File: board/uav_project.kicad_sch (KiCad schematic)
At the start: 0 parts

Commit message: Hopefully finished schema for pcb
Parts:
- added C14: 100n, symbol Device:C
- added D5: RCLAMP3328P, Package_DFN_QFN:UDFN-9_1.0x3.8mm_P0.5mm, symbol Power_Protection:RCLAMP3328P
- added J2: Conn_01x08_Pin, symbol Connector:Conn_01x08_Pin
- added R24, R25: 4.7k, symbol Device:R
- added WT901B1: ~, symbol .kicad_sym:WT901B
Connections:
- new net: D5.9 (K8), J2.8 (Pin_8)
- new net +3V3: C14.1, D5.8 (K7), J2.7 (Pin_7), R24.1, R25.1, WT901B1. (VCC)
- new net +5V: D5.7 (K6), J2.6 (Pin_6)
- new net DX: D5.2 (K2), J2.2 (Pin_2)
- new net GND: C14.2, D5.3 (A), D5.6 (K5), J2.5 (Pin_5), WT901B1. (VCC)
- new net SDA: D5.4 (K3), J2.3 (Pin_3), R24.2, WT901B1. (VCC)
- new net SLC: D5.5 (K4), J2.4 (Pin_4), R25.2, WT901B1. (VCC)
- new net TX: D5.1 (K1), J2.1 (Pin_1)
- no-connect marks 0 -> 6
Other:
- note added: "Connection"
- note added: "I2C pullup"
- note added: "WT901B"

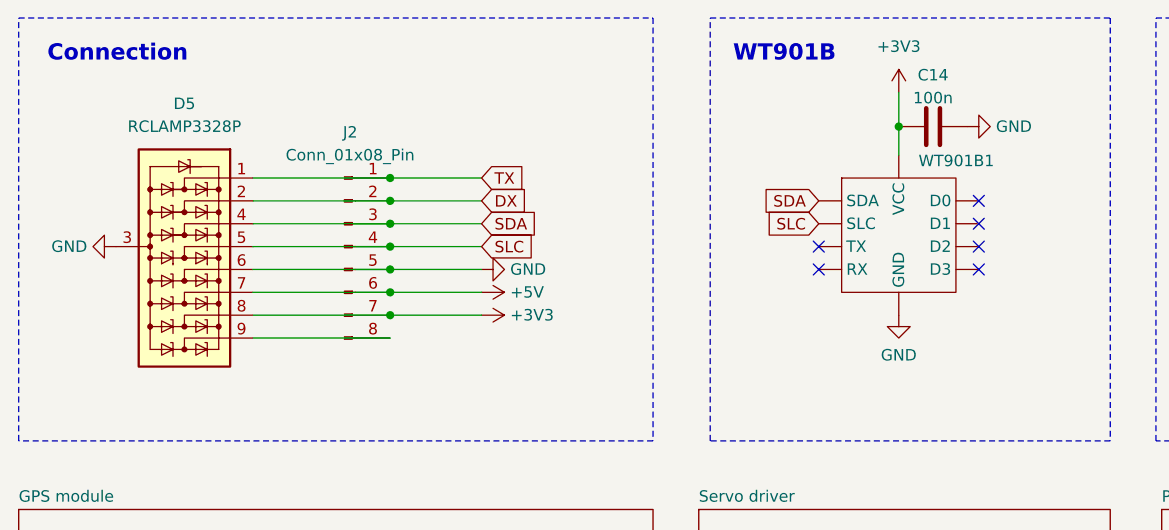
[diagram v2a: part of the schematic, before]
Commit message: Updated schme to comply with electrical rules checker, prepared sensor logic for rewrite
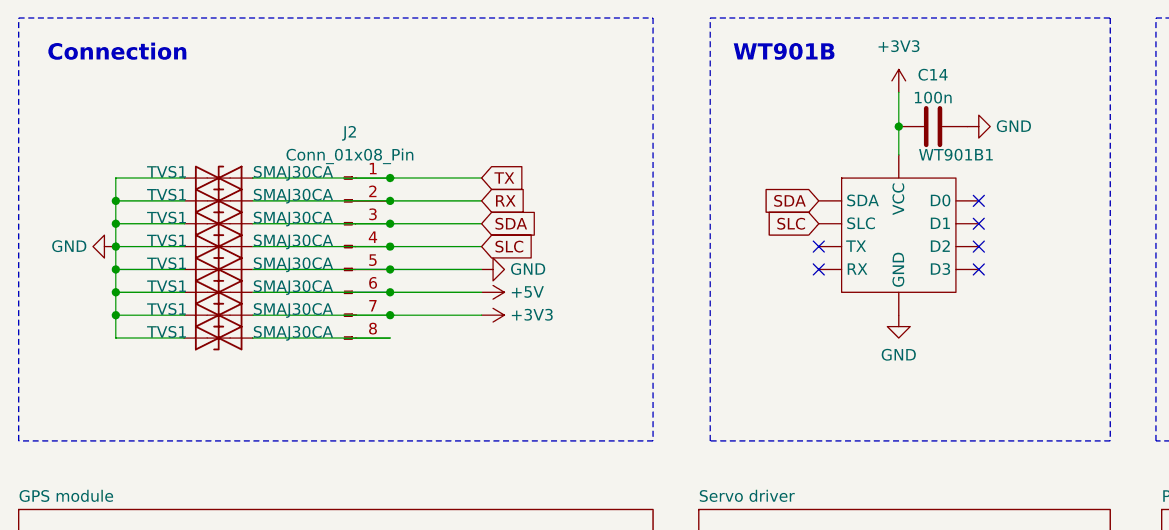
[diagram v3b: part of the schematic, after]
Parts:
- removed D5: RCLAMP3328P, Package_DFN_QFN:UDFN-9_1.0x3.8mm_P0.5mm, symbol Power_Protection:RCLAMP3328P
- removed WT901B1: ~, symbol .kicad_sym:WT901B
- added TVS1 (x8): SMAJ30CA, Diode_SMD:D_SMA, symbol Diode:SMAJ30CA
- added WT901B1: ~, Custom_Footprints:WT901B, symbol Custom_Symbols:WT901B
- C14: footprint (none) -> Capacitor_SMD:C_0603_1608Metric
- J2: footprint (none) -> Connector_IDC:IDC-Header_2x04_P2.54mm_Vertical
- R24, R25: footprint (none) -> Resistor_SMD:R_0603_1608Metric
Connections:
- net +3V3: now also TVS1.1 (A1), WT901B1. (VCC)
- net +5V: now also TVS1.1 (A1)
- net GND: now also TVS1.1 (A1), TVS1.2 (A2), TVS1.2 (A2), TVS1.2 (A2), TVS1.2 (A2), TVS1.2 (A2), TVS1.2 (A2), TVS1.2 (A2), TVS1.2 (A2), WT901B1. (VCC)
- net SDA: now also TVS1.1 (A1), WT901B1. (VCC)
- net SLC: now also TVS1.1 (A1), WT901B1. (VCC)
- net TX: now also TVS1.1 (A1)
- net at J2.8 (Pin_8): now also TVS1.1 (A1)
- net DX renamed RX
- net RX: now also TVS1.1 (A1)
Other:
- title: (none) -> Root page UAV board

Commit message: Started work on PCB design, more work on rewritting firmware to be semi usable
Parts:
- added H1, H2, H3, H4: MountingHole, MountingHole:MountingHole_2.2mm_M2, symbol Mechanical:MountingHole
- J2: footprint Connector_IDC:IDC-Header_2x04_P2.54mm_Vertical -> Connector_PinHeader_1.00mm:PinHeader_1x08_P1.00mm_Vertical
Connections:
- net +3V3: now also WT901B1.2 (VCC); no longer WT901B1. (VCC)
- net GND: now also WT901B1.5 (GND); no longer WT901B1. (VCC)
- net SDA: now also WT901B1.9 (SDA); no longer WT901B1. (VCC)
- net SLC: now also WT901B1.8 (SLC); no longer WT901B1. (VCC)
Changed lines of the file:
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@@
-    )
-  )
-  (symbol (lib_id "Custom_Symbols:WT901B") (at 159.385 67.31 0) (unit 1)
-    (in_bom yes) (on_board yes) (dnp no) (fields_autoplaced)
-    (property "Reference" "WT901B1" (at 161.5791 66.04 0)
-      (effects (font (size 1.27 1.27)) (justify left))
-    )
-    (property "Value" "~" (at 159.385 67.31 0)
-      (effects (font (size 1.27 1.27)))
-    )
-    (property "Footprint" "Custom_Footprints:WT901B" (at 159.385 67.31 0)
-      (effects (font (size 1.27 1.27)) hide)
-    )
-    (property "Datasheet" "" (at 159.385 67.31 0)
-      (effects (font (size 1.27 1.27)) hide)
-    )
-    (pin "")
-    (pin "")
-    (pin "")
-    (pin "")
-    (pin "")
-    (pin "")
-    (pin "")
-    (pin "")
-    (pin "")
-    (pin "")
-    (instances
-      (project "uav_project"
-        (path "/a8bf0924-b264-4c19-8c7e-9c0e131cacba"
-          (reference "WT901B1") (unit 1)
-        )
-      )
     )
   )
@@
     )
   )
+  (symbol (lib_id "Mechanical:MountingHole") (at 87.63 94.615 0) (unit 1)
+    (in_bom yes) (on_board yes) (dnp no) (fields_autoplaced)
+    (property "Reference" "H4" (at 90.17 93.345 0)
+      (effects (font (size 1.27 1.27)) (justify left))
+    )
+    (property "Value" "MountingHole" (at 90.17 95.885 0)
+      (effects (font (size 1.27 1.27)) (justify left) hide)
+    )
+    (property "Footprint" "MountingHole:MountingHole_2.2mm_M2" (at 87.63 94.615 0)
+      (effects (font (size 1.27 1.27)) hide)
+    )
+    (property "Datasheet" "~" (at 87.63 94.615 0)
+      (effects (font (size 1.27 1.27)) hide)
+    )
+    (instances
+      (project "uav_project"
+        (path "/a8bf0924-b264-4c19-8c7e-9c0e131cacba"
+          (reference "H4") (unit 1)
+        )
+      )
+    )
+  )
   (symbol (lib_id "Connector:Conn_01x08_Pin") (at 97.79 76.2 0) (unit 1)
     (in_bom yes) (on_board yes) (dnp no) (fields_autoplaced)
@@
       (effects (font (size 1.27 1.27)))
     )
-    (property "Footprint" "Connector_IDC:IDC-Header_2x04_P2.54mm_Vertical" (at 97.79 76.2 0)
+    (property "Footprint" "Connector_PinHeader_1.00mm:PinHeader_1x08_P1.00mm_Vertical" (at 97.79 76.2 0)
       (effects (font (size 1.27 1.27)) hide)
     )
@@
     )
   )
+  (symbol (lib_id "Mechanical:MountingHole") (at 80.01 94.615 0) (unit 1)
+    (in_bom yes) (on_board yes) (dnp no) (fields_autoplaced)
+    (property "Reference" "H3" (at 82.55 93.345 0)
+      (effects (font (size 1.27 1.27)) (justify left))
+    )
+    (property "Value" "MountingHole" (at 82.55 95.885 0)
+      (effects (font (size 1.27 1.27)) (justify left) hide)
+    )
+    (property "Footprint" "MountingHole:MountingHole_2.2mm_M2" (at 80.01 94.615 0)
+      (effects (font (size 1.27 1.27)) hide)
+    )
+    (property "Datasheet" "~" (at 80.01 94.615 0)
+      (effects (font (size 1.27 1.27)) hide)
+    )
+    (instances
+      (project "uav_project"
+        (path "/a8bf0924-b264-4c19-8c7e-9c0e131cacba"
+          (reference "H3") (unit 1)
+        )
+      )
+    )
+  )
   (symbol (lib_id "power:GND") (at 72.39 76.2 270) (unit 1)
     (in_bom yes) (on_board yes) (dnp no) (fields_autoplaced)
@@
     )
   )
+  (symbol (lib_id "Mechanical:MountingHole") (at 64.77 94.615 0) (unit 1)
+    (in_bom yes) (on_board yes) (dnp no) (fields_autoplaced)
+    (property "Reference" "H1" (at 67.31 93.345 0)
+      (effects (font (size 1.27 1.27)) (justify left))
+    )
+    (property "Value" "MountingHole" (at 67.31 95.885 0)
+      (effects (font (size 1.27 1.27)) (justify left) hide)
+    )
+    (property "Footprint" "MountingHole:MountingHole_2.2mm_M2" (at 64.77 94.615 0)
+      (effects (font (size 1.27 1.27)) hide)
+    )
+    (property "Datasheet" "~" (at 64.77 94.615 0)
+      (effects (font (size 1.27 1.27)) hide)
+    )
+    (instances
+      (project "uav_project"
+        (path "/a8bf0924-b264-4c19-8c7e-9c0e131cacba"
+          (reference "H1") (unit 1)
+        )
+      )
+    )
+  )
   (symbol (lib_id "power:GND") (at 159.385 83.82 0) (unit 1)
     (in_bom yes) (on_board yes) (dnp no) (fields_autoplaced)
@@
         (path "/a8bf0924-b264-4c19-8c7e-9c0e131cacba"
           (reference "#PWR068") (unit 1)
+        )
+      )
+    )
+  )
+  (symbol (lib_id "Custom_Symbols:WT901B") (at 159.385 67.31 0) (unit 1)
+    (in_bom yes) (on_board yes) (dnp no) (fields_autoplaced)
+    (property "Reference" "WT901B1" (at 161.5791 66.04 0)
+      (effects (font (size 1.27 1.27)) (justify left))
+    )
+    (property "Value" "~" (at 159.385 67.31 0)
+      (effects (font (size 1.27 1.27)))
+    )
+    (property "Footprint" "Custom_Footprints:WT901B" (at 159.385 67.31 0)
+      (effects (font (size 1.27 1.27)) hide)
+    )
+    (property "Datasheet" "" (at 159.385 67.31 0)
+      (effects (font (size 1.27 1.27)) hide)
+    )
+    (pin "1")
+    (pin "10")
+    (pin "2")
+    (pin "3")
+    (pin "4")
+    (pin "5")
+    (pin "6")
+    (pin "7")
+    (pin "8")
+    (pin "9")
+    (instances
+      (project "uav_project"
+        (path "/a8bf0924-b264-4c19-8c7e-9c0e131cacba"
+          (reference "WT901B1") (unit 1)
         )
       )
@@
         )
       )
+    )
+  )
+  (symbol (lib_id "Mechanical:MountingHole") (at 72.39 94.615 0) (unit 1)
+    (in_bom yes) (on_board yes) (dnp no) (fields_autoplaced)
+    (property "Reference" "H2" (at 74.93 93.345 0)
+      (effects (font (size 1.27 1.27)) (justify left))
+    )
+    (property "Value" "MountingHole" (at 74.93 95.885 0)
+      (effects (font (size 1.27 1.27)) (justify left) hide)
+    )
+    (property "Footprint" "MountingHole:MountingHole_2.2mm_M2" (at 72.39 94.615 0)
+      (effects (font (size 1.27 1.27)) hide)
+    )
+    (property "Datasheet" "~" (at 72.39 94.615 0)
+      (effects (font (size 1.27 1.27)) hide)
+    )
+    (instances
+      (project "uav_project"
+        (path "/a8bf0924-b264-4c19-8c7e-9c0e131cacba"
+          (reference "H2") (unit 1)
+        )
+      )

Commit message: More work on PCB design
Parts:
- removed J2: Conn_01x08_Pin, Connector_PinHeader_1.00mm:PinHeader_1x08_P1.00mm_Vertical, symbol Connector:Conn_01x08_Pin
- removed TVS1: SMAJ30CA, Diode_SMD:D_SMA, symbol Diode:SMAJ30CA
- added J1: Conn_01x07, Connector_PinHeader_1.00mm:PinHeader_1x07_P1.00mm_Vertical, symbol Connector_Generic:Conn_01x07
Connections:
- net +3V3: now also TVS1.1 (A1), J1.3 (Pin_3); no longer TVS1.1 (A1)
- net +5V: now also TVS1.1 (A1), J1.2 (Pin_2); no longer TVS1.1 (A1)
- net GND: now also TVS1.1 (A1), J1.1 (Pin_1); no longer TVS1.1 (A1)
- net RX: now also TVS1.1 (A1), J1.5 (Pin_5); no longer TVS1.1 (A1)
- net SDA: now also TVS1.1 (A1), J1.6 (Pin_6); no longer TVS1.1 (A1)
- net SLC: now also TVS1.1 (A1), J1.7 (Pin_7); no longer TVS1.1 (A1)
- net TX: now also TVS1.1 (A1), J1.4 (Pin_4); no longer TVS1.1 (A1)

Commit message: First version of PCB finished
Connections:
- net RX: now also J1.7 (Pin_7), TVS1.1 (A1); no longer J1.5 (Pin_5), TVS1.1 (A1)
- net SDA: now also J1.4 (Pin_4), TVS1.1 (A1); no longer J1.6 (Pin_6), TVS1.1 (A1)
- net SLC: now also J1.5 (Pin_5), TVS1.1 (A1); no longer J1.7 (Pin_7), TVS1.1 (A1)
- net TX: now also J1.6 (Pin_6), TVS1.1 (A1); no longer J1.4 (Pin_4), TVS1.1 (A1)
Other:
- note added: "0x50"
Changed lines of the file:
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@@
     (fill (type none))
+  )
+  (text "0x50" (at 140.97 59.055 0)
+    (effects (font (size 1.8 1.8) bold) (justify left bottom))
   )
   (text "WT901B" (at 140.97 55.88 0)
@@
     )
   )
-  (global_label "SDA" (shape input) (at 113.03 81.28 0) (fields_autoplaced)
+  (global_label "SDA" (shape input) (at 113.03 76.2 0) (fields_autoplaced)
     (effects (font (size 1.27 1.27)) (justify left))
-    (property "Intersheetrefs" "${INTERSHEET_REFS}" (at 119.5833 81.28 0)
+    (property "Intersheetrefs" "${INTERSHEET_REFS}" (at 119.5833 76.2 0)
+      (effects (font (size 1.27 1.27)) (justify left) hide)
+    )
+  )
+  (global_label "TX" (shape input) (at 113.03 81.28 0) (fields_autoplaced)
+    (effects (font (size 1.27 1.27)) (justify left))
+    (property "Intersheetrefs" "${INTERSHEET_REFS}" (at 118.1923 81.28 0)
+      (effects (font (size 1.27 1.27)) (justify left) hide)
+    )
+  )
+  (global_label "RX" (shape input) (at 113.03 83.82 0) (fields_autoplaced)
+    (effects (font (size 1.27 1.27)) (justify left))
+    (property "Intersheetrefs" "${INTERSHEET_REFS}" (at 118.4947 83.82 0)
       (effects (font (size 1.27 1.27)) (justify left) hide)
     )
@@
     )
   )
-  (global_label "SLC" (shape input) (at 113.03 83.82 0) (fields_autoplaced)
+  (global_label "SLC" (shape input) (at 113.03 78.74 0) (fields_autoplaced)
     (effects (font (size 1.27 1.27)) (justify left))
-    (property "Intersheetrefs" "${INTERSHEET_REFS}" (at 119.5228 83.82 0)
-      (effects (font (size 1.27 1.27)) (justify left) hide)
-    )
-  )
-  (global_label "TX" (shape input) (at 113.03 76.2 0) (fields_autoplaced)
-    (effects (font (size 1.27 1.27)) (justify left))
-    (property "Intersheetrefs" "${INTERSHEET_REFS}" (at 118.1923 76.2 0)
-      (effects (font (size 1.27 1.27)) (justify left) hide)
-    )
-  )
-  (global_label "RX" (shape input) (at 113.03 78.74 0) (fields_autoplaced)
-    (effects (font (size 1.27 1.27)) (justify left))
-    (property "Intersheetrefs" "${INTERSHEET_REFS}" (at 118.4947 78.74 0)
+    (property "Intersheetrefs" "${INTERSHEET_REFS}" (at 119.5228 78.74 0)
       (effects (font (size 1.27 1.27)) (justify left) hide)
     )
@@
   )
   (symbol (lib_id "power:+3V3") (at 113.03 73.66 270) (unit 1)
-    (in_bom yes) (on_board yes) (dnp no) (fields_autoplaced)
+    (in_bom yes) (on_board yes) (dnp no)
     (property "Reference" "#PWR072" (at 109.22 73.66 0)
       (effects (font (size 1.27 1.27)) hide)

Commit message: Minor improvements to board design
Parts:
- removed TVS1: SMAJ30CA, Diode_SMD:D_SMA, symbol Diode:SMAJ30CA
- removed WT901B1: ~, Custom_Footprints:WT901B, symbol Custom_Symbols:WT901B
- added U7: WT901B, Custom_Footprints:WT901B, symbol Custom_Symbols:WT901B
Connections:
- net +3V3: now also J1.2 (Pin_2), TVS1.1 (A1), U7.2 (VCC); no longer J1.3 (Pin_3), TVS1.1 (A1)
- net +5V: now also J1.3 (Pin_3), TVS1.1 (A1); no longer J1.2 (Pin_2), TVS1.1 (A1)
- net GND: now also U7.5 (GND)
- net SDA: now also U7.9 (SDA)
- net SLC: now also U7.8 (SLC)
